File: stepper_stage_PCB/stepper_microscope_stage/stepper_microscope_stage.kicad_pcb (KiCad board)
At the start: 2 copper layers, 119.9 x 159.6 mm, 27 parts, among them J2 Conn_01x04_Socket, J2 Screw_Terminal_01x04, J3 Screw_Terminal_01x04, J4 Conn_01x04_Socket, J5 Conn_01x04_Socket, SW1 SW_SPDT

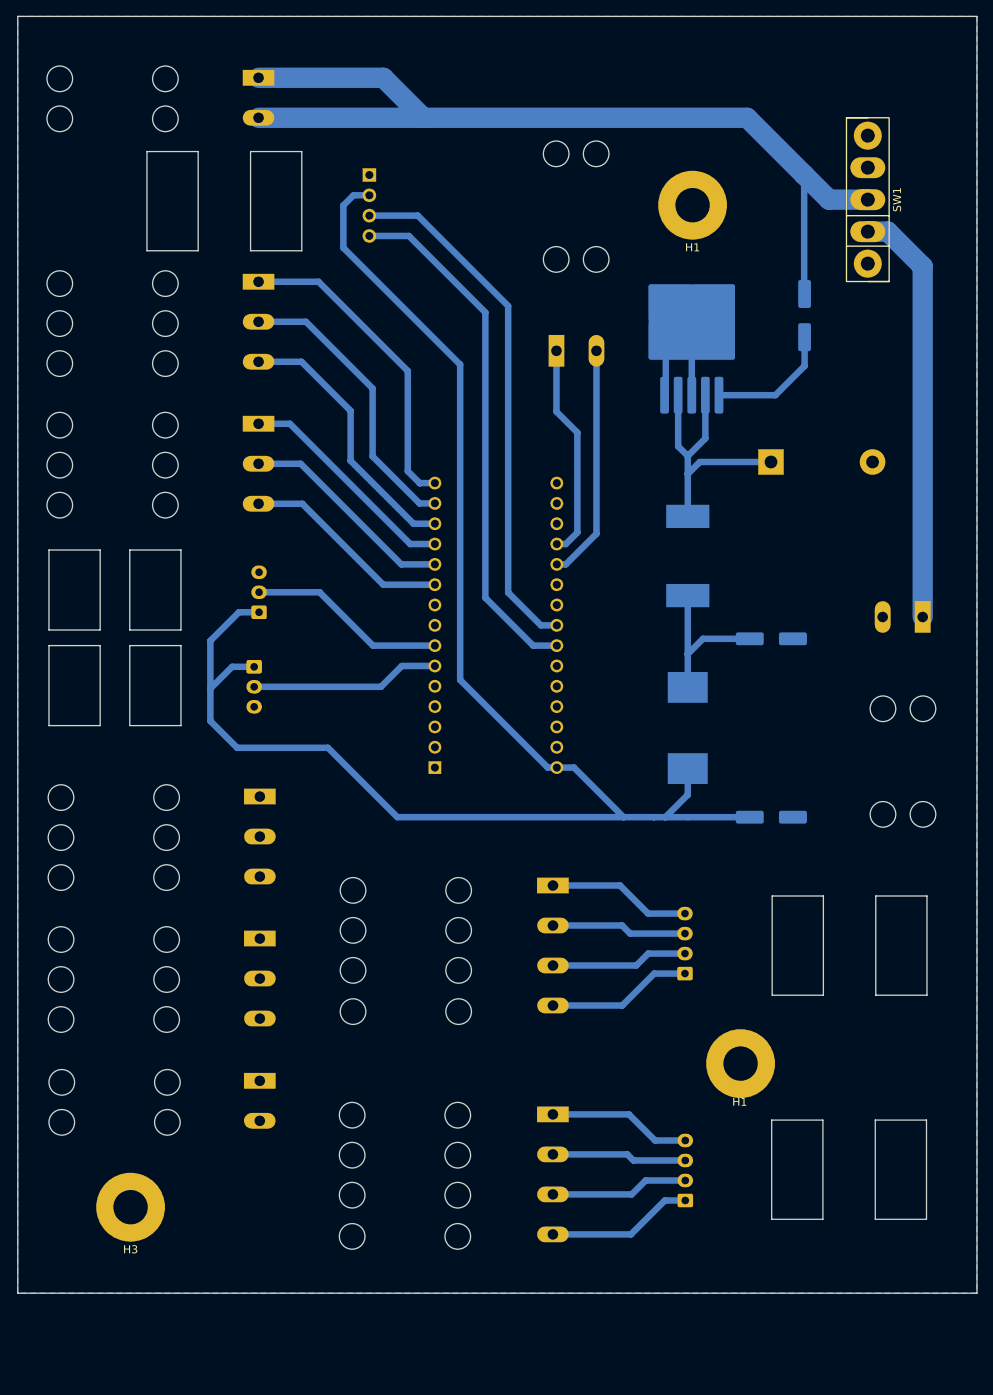
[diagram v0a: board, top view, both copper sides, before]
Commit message: Version 0
Updated PCB, milled that PCB, soldered parts to that PCB, updated code, works as expected except for the following functionalities listed below:
- Laser gates are non-operational as of yet. This leads to the following:
	- No homing functionality yet
	- No safety measures to ensure the steppers avoid grinding on their bearings
- True logarithmic speed control
- Suitable housing
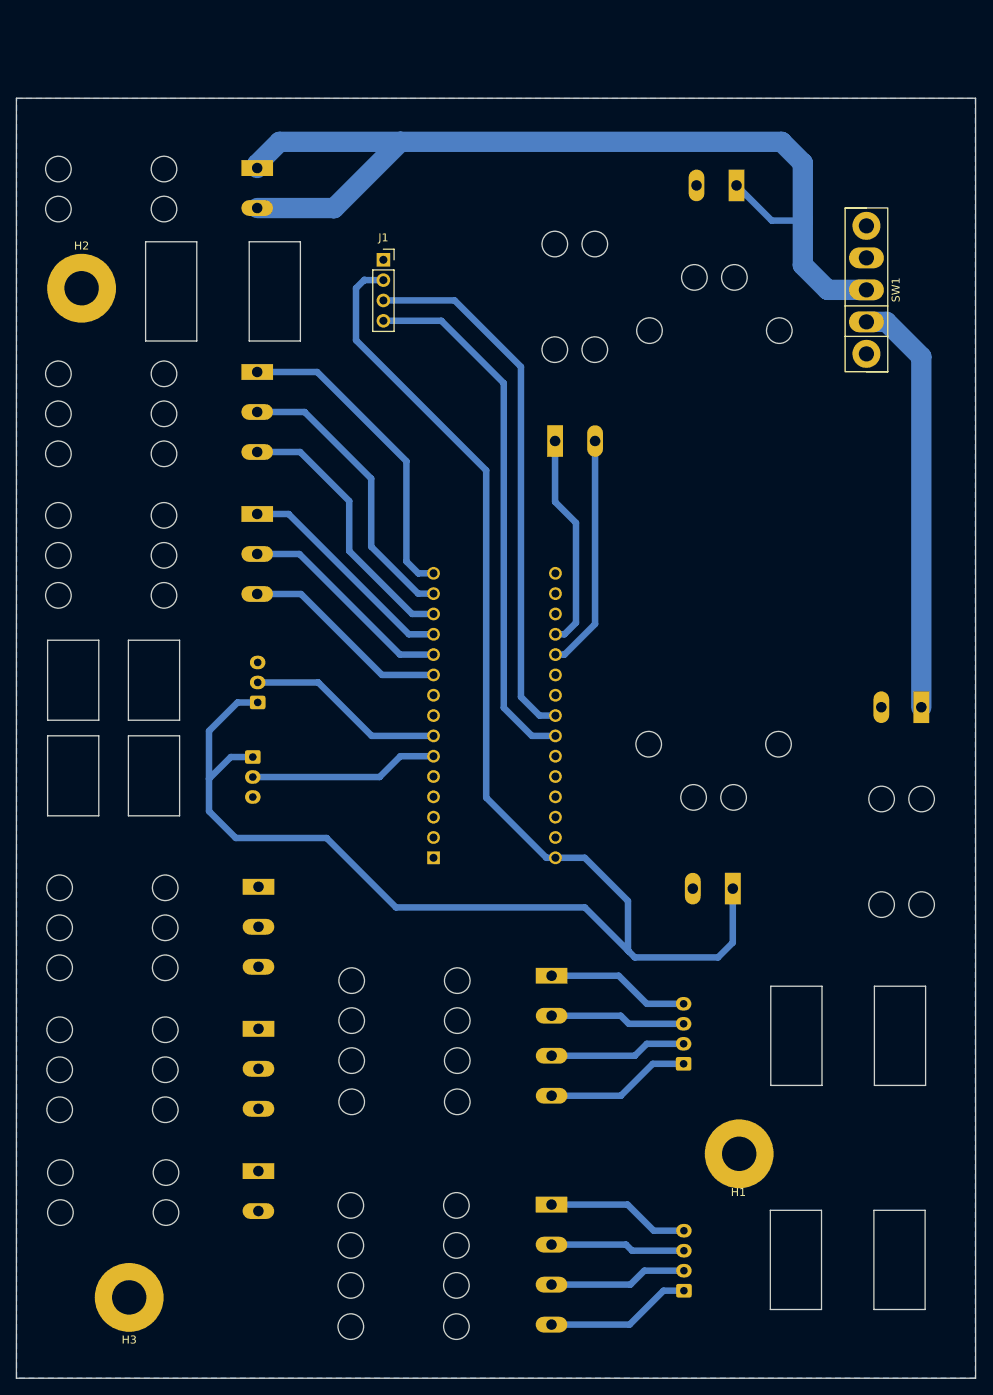
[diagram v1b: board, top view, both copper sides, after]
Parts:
- removed C1, C3: 100uF, Capacitor_SMD:CP_Elec_6.3x7.7
- removed C2: 330uF, Capacitor_SMD:CP_Elec_6.3x7.7
- removed D1: 1N5821, Diode_THT:D_DO-201AD_P12.70mm_Horizontal
- removed the H1 at (124.0, 38.8)
- removed the J2 at (83.6, 35.0)
- removed L1: 330uH, Inductor_SMD:L_12x12mm_H6mm
- removed L2: 20uH, Inductor_SMD:L_Wuerth_HCI-1335
- removed TL2575: U1, Package_TO_SOT_SMD:TO-263-5_TabPin3
- added BUCKVIN1: Screw_Terminal_01x02, TerminalBlock:TerminalBlock_Altech_AK300-2_P5.00mm, B.Cu at (129.5, 36.3)
- added BUCKVOUT1: Screw_Terminal_01x02, TerminalBlock:TerminalBlock_Altech_AK300-2_P5.00mm, B.Cu at (129.0, 124.2)
- added H2: MountingHole_Pad, MountingHole:MountingHole_4.3mm_M4_Pad, F.Cu at (47.6, 49.1)
- added J1: Conn_01x04_Socket, Connector_PinSocket_2.54mm:PinSocket_1x04_P2.54mm_Vertical, F.Cu at (85.4, 45.6)
- moved H3 11.3 mm to (53.6, 175.3)
- moved J4 11.3 mm to (122.9, 174.4)
- moved STEPPWR1 11.3 mm to (69.6, 34.1)
- moved A1 11.3 mm to (91.6, 120.3)
- moved J3 11.3 mm to (106.4, 135.1)
- moved JOYIN1 11.3 mm to (106.8, 68.2)
- moved LIMIT1 11.3 mm to (69.6, 100.9)
- moved LIMIT2 11.3 mm to (69.0, 107.7)
- moved STEPSIG1 11.3 mm to (69.6, 59.6)
- moved STEPSIG2 11.3 mm to (69.6, 77.3)
- moved STEPSIGGND1 11.3 mm to (69.7, 124.0)
- moved SW1 11.3 mm to (145.7, 49.3)
- moved VIN1 11.3 mm to (152.6, 101.5)
- moved H1 11.3 mm to (129.8, 157.3)
- moved J2 11.3 mm to (106.4, 163.7)
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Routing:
- net Net-(D1-K): track 35.2 -> 0.00 mm
- net Net-(C2-Pad1): track 20.0 -> 0.00 mm
- net GND: track 16.9 -> 0.79 mm
- net Net-(TL2575-+Vin): track 15.8 -> 0.00 mm
- net +5V: track 200.5 -> 208.5 mm
- net +24V: track 170.5 -> 176.9 mm
- net Net-(A1-A4): track 65.6 -> 67.2 mm
- net Net-(A1-A5): track 65.5 -> 66.8 mm
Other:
- board size 119.9 x 159.6 mm -> 119.9 x 160 mm
